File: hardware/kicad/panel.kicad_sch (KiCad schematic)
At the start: 1 part

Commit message: Schematic: panel sheet with 48 lamps
6x 74HC595 (U14-U19) sinking 48 lamps (D7-D54) from VLED through 2k2 x4
arrays (RN1-RN12); chain via QH' local labels; OE_N pull-up. Lamp order
matches firmware/src/panel.h. Custom 595 symbol puts ~SRCLR on top so it
ties to +3V3 without crossings. check.py no longer has pending nets.

Co-Authored-By: Claude Opus 5.5 <noreply@anthropic.com>
Claude-Session: https://claude.ai/code/session_01YRUiF8Vp4242sya9Xyg3TV
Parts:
- added C41, C42, C43, C44, C45, C46: 100nF/16V/10%, Capacitor_SMD:C_0603_1608Metric, symbol Device:C
- added D10, D11, D12, D13, D14, D15, D16, D17, D18, D19, D20, D21, D22, D23, D24, D25, D26, D27, D28, D29, D30, D43, D7, D8, D9: AMBER(0603), LED_SMD:LED_0603_1608Metric, symbol Device:LED
- added D31, D32, D41, D42, D44, D51, D53: YELLOW(0603), LED_SMD:LED_0603_1608Metric, symbol Device:LED
- added D33, D40, D45, D48, D49: GREEN(0603), LED_SMD:LED_0603_1608Metric, symbol Device:LED
- added D34, D35, D36, D37, D38, D39, D46, D47, D50, D52, D54: RED(0603), LED_SMD:LED_0603_1608Metric, symbol Device:LED
- added RN1, RN10, RN11, RN12, RN2, RN3, RN4, RN5, RN6, RN7, RN8, RN9: 2k2x4/5%(CAY16), Resistor_SMD:R_Array_Convex_4x0603, symbol Device:R_Pack04
- added U14, U15, U16, U17, U18, U19: 74HC595PW(TSSOP16), Package_SO:TSSOP-16_4.4x5mm_P0.65mm, symbol coaxolotl:74HC595
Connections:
- net +3V3: now also C41.1, C42.1, C43.1, C44.1, C45.1, C46.1, U14.10 (~{SRCLR}), U14.16 (VCC), U15.10 (~{SRCLR}), U15.16 (VCC), U16.10 (~{SRCLR}), U16.16 (VCC), U17.10 (~{SRCLR}), U17.16 (VCC), U18.10 (~{SRCLR}), U18.16 (VCC), U19.10 (~{SRCLR}), U19.16 (VCC)
- net LED_OE_N: now also U14.13 (~{OE}), U15.13 (~{OE}), U16.13 (~{OE}), U17.13 (~{OE}), U18.13 (~{OE}), U19.13 (~{OE})
- net LED_RCK: now also U14.12 (RCLK), U15.12 (RCLK), U16.12 (RCLK), U17.12 (RCLK), U18.12 (RCLK), U19.12 (RCLK)
- net LED_SCK: now also U14.11 (SRCLK), U15.11 (SRCLK), U16.11 (SRCLK), U17.11 (SRCLK), U18.11 (SRCLK), U19.11 (SRCLK)
- net LED_SER: now also U14.14 (SER)
- new net: D19.1 (K), RN4.8 (R1.2)
- new net: D22.1 (K), RN4.5 (R4.2)
- new net: D18.1 (K), RN3.5 (R4.2)
- new net: D24.1 (K), RN5.7 (R2.2)
- new net: D10.1 (K), RN1.5 (R4.2)
- new net: RN12.1 (R1.1), U19.4 (QE)
- new net: RN12.2 (R2.1), U19.5 (QF)
- new net: RN12.3 (R3.1), U19.6 (QG)
- new net: RN12.4 (R4.1), U19.7 (QH)
- new net: D54.1 (K), RN12.5 (R4.2)
- new net: D53.1 (K), RN12.6 (R3.2)
- new net: D52.1 (K), RN12.7 (R2.2)
- new net: D51.1 (K), RN12.8 (R1.2)
- new net: D39.1 (K), RN9.8 (R1.2)
- new net: D21.1 (K), RN4.6 (R3.2)
- new net: D46.1 (K), RN10.5 (R4.2)
- new net: RN10.1 (R1.1), U18.4 (QE)
- new net: RN10.2 (R2.1), U18.5 (QF)
- new net: RN10.3 (R3.1), U18.6 (QG)
- new net: RN10.4 (R4.1), U18.7 (QH)
- new net: D45.1 (K), RN10.6 (R3.2)
- new net: D44.1 (K), RN10.7 (R2.2)
- new net: D43.1 (K), RN10.8 (R1.2)
- new net: D16.1 (K), RN3.7 (R2.2)
- new net: D9.1 (K), RN1.6 (R3.2)
- new net: D42.1 (K), RN9.5 (R4.2)
- new net: D33.1 (K), RN7.6 (R3.2)
- new net: D32.1 (K), RN7.7 (R2.2)
- new net: RN9.1 (R1.1), U18.15 (QA)
- new net: RN9.2 (R2.1), U18.1 (QB)
- new net: RN9.3 (R3.1), U18.2 (QC)
- new net: RN9.4 (R4.1), U18.3 (QD)
- new net: D41.1 (K), RN9.6 (R3.2)
- new net: D40.1 (K), RN9.7 (R2.2)
- new net: D28.1 (K), RN6.7 (R2.2)
- new net: RN7.1 (R1.1), U17.15 (QA)
- new net: RN7.2 (R2.1), U17.1 (QB)
- new net: RN7.3 (R3.1), U17.2 (QC)
- new net: RN7.4 (R4.1), U17.3 (QD)
- new net: D34.1 (K), RN7.5 (R4.2)
- new net: D31.1 (K), RN7.8 (R1.2)
- new net: RN4.1 (R1.1), U15.4 (QE)
- new net: RN4.2 (R2.1), U15.5 (QF)
- new net: RN4.3 (R3.1), U15.6 (QG)
- new net: RN4.4 (R4.1), U15.7 (QH)
- new net: D20.1 (K), RN4.7 (R2.2)
- new net: RN11.1 (R1.1), U19.15 (QA)
- new net: RN11.2 (R2.1), U19.1 (QB)
- new net: RN11.3 (R3.1), U19.2 (QC)
- new net: RN11.4 (R4.1), U19.3 (QD)
- new net: D50.1 (K), RN11.5 (R4.2)
- new net: D49.1 (K), RN11.6 (R3.2)
- new net: D48.1 (K), RN11.7 (R2.2)
- new net: D47.1 (K), RN11.8 (R1.2)
- new net: RN1.2 (R2.1), U14.1 (QB)
- new net: RN1.1 (R1.1), U14.15 (QA)
- new net: RN1.3 (R3.1), U14.2 (QC)
- new net: RN1.4 (R4.1), U14.3 (QD)
- new net: RN2.1 (R1.1), U14.4 (QE)
- new net: RN2.2 (R2.1), U14.5 (QF)
- new net: RN2.3 (R3.1), U14.6 (QG)
- new net: RN2.4 (R4.1), U14.7 (QH)
- new net: RN8.1 (R1.1), U17.4 (QE)
- new net: RN8.2 (R2.1), U17.5 (QF)
- new net: RN8.3 (R3.1), U17.6 (QG)
- new net: RN8.4 (R4.1), U17.7 (QH)
- new net: D14.1 (K), RN2.5 (R4.2)
- new net: RN3.1 (R1.1), U15.15 (QA)
- new net: RN3.2 (R2.1), U15.1 (QB)
- new net: RN3.3 (R3.1), U15.2 (QC)
- new net: RN3.4 (R4.1), U15.3 (QD)
- new net: D17.1 (K), RN3.6 (R3.2)
- new net: D15.1 (K), RN3.8 (R1.2)
- new net: D29.1 (K), RN6.6 (R3.2)
- new net: D36.1 (K), RN8.7 (R2.2)
- new net: D8.1 (K), RN1.7 (R2.2)
- new net: D26.1 (K), RN5.5 (R4.2)
- new net: D38.1 (K), RN8.5 (R4.2)
- new net: D37.1 (K), RN8.6 (R3.2)
- new net: D35.1 (K), RN8.8 (R1.2)
- new net: D7.1 (K), RN1.8 (R1.2)
- new net: D27.1 (K), RN6.8 (R1.2)
- new net: D25.1 (K), RN5.6 (R3.2)
- new net: RN5.2 (R2.1), U16.1 (QB)
- new net: RN5.1 (R1.1), U16.15 (QA)
- new net: RN5.3 (R3.1), U16.2 (QC)
- new net: RN5.4 (R4.1), U16.3 (QD)
- new net: RN6.1 (R1.1), U16.4 (QE)
- new net: RN6.2 (R2.1), U16.5 (QF)
- new net: RN6.3 (R3.1), U16.6 (QG)
- new net: RN6.4 (R4.1), U16.7 (QH)
- new net: D13.1 (K), RN2.6 (R3.2)
- new net: D12.1 (K), RN2.7 (R2.2)
- new net: D11.1 (K), RN2.8 (R1.2)
- new net: D23.1 (K), RN5.8 (R1.2)
- new net: D30.1 (K), RN6.5 (R4.2)
- new net GND: C41.2, C42.2, C43.2, C44.2, C45.2, C46.2, U14.8 (GND), U15.8 (GND), U16.8 (GND), U17.8 (GND), U18.8 (GND), U19.8 (GND)
- new net LED_CH1: U14.9 (QH'), U15.14 (SER)
- new net LED_CH2: U15.9 (QH'), U16.14 (SER)
- new net LED_CH3: U16.9 (QH'), U17.14 (SER)
- new net LED_CH4: U17.9 (QH'), U18.14 (SER)
- new net LED_CH5: U18.9 (QH'), U19.14 (SER)
- new net VLED: D10.2 (A), D11.2 (A), D12.2 (A), D13.2 (A), D14.2 (A), D15.2 (A), D16.2 (A), D17.2 (A), D18.2 (A), D19.2 (A), D20.2 (A), D21.2 (A), D22.2 (A), D23.2 (A), D24.2 (A), D25.2 (A), D26.2 (A), D27.2 (A), D28.2 (A), D29.2 (A), D30.2 (A), D31.2 (A), D32.2 (A), D33.2 (A), D34.2 (A), D35.2 (A), D36.2 (A), D37.2 (A), D38.2 (A), D39.2 (A), D40.2 (A), D41.2 (A), D42.2 (A), D43.2 (A), D44.2 (A), D45.2 (A), D46.2 (A), D47.2 (A), D48.2 (A), D49.2 (A), D50.2 (A), D51.2 (A), D52.2 (A), D53.2 (A), D54.2 (A), D7.2 (A), D8.2 (A), D9.2 (A)
- no-connect marks 0 -> 1
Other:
- note added: "0 F0 THRU"
- note added: "1 F1 LF"
- note added: "10 FR2 SYNC"
- note added: "11 FR3 B2"
- note added: "12 FR4 B1"
- note added: "13 FR5 B0"
- note added: "14 FR6 LNA"
- note added: "15 FR7 QUIET"
- note added: "16 FR8 CLR"
- note added: "17 FR9 CHK"
- note added: "18 FR10 CHK"
- note added: "19 FR11 CHK"
- note added: "2 F2 160/80"
- note added: "20 FR12 CHK"
- note added: "21 FR13 CHK"
- note added: "22 FR14 CHK"
- note added: "23 RX"
- note added: "24 0"
- note added: "25 1"
- note added: "26 OK"
- note added: "27 ERR"
- note added: "28 SYNC"
- note added: "29 CHK"
- note added: "3 F3 60-30"
- note added: "30 GAP"
- note added: "31 RUNT"
- note added: "32 TMO"
- note added: "33 LNA"
- note added: "34 BYP"
- note added: "35 AUTO"
- note added: "36 FMN"
- note added: "37 I-LO"
- note added: "38 I-OK"
- note added: "39 I-HI"
- note added: "4 F4 20-10"
- note added: "40 TRIP"
- note added: "41 RUN"
- note added: "42 HOLD"
- note added: "43 LOW"
- note added: "44 QUIET"
- note added: "45 DROP"
- note added: "46 GLT"
- note added: "47 RST"
- note added: "5 F5 6/4m"
- note added: "6 F6 2m/AIR"
- note added: "7 F7 70/23cm"
- note added: "8 FR0 SYNC"
- note added: "9 FR1 SYNC"
- note added: "BANK (lamps 0-7)"
- note added: "DECODE (lamps 24-31)"
- note added: "DECODE + RF (lamps 32-39)"
- note added: "FRAME (lamps 8-15)"
- note added: "FRAME + RX (lamps 16-23)"
- note added: "Lamp n: register n/8 (U14 = first after the MCU), output Q(n%8) - firmware/src/panel.h."
- note added: "Lamp test lights all 48 (48 mA) with the LNA still off. Outside it, at most 23 lamps."
- note added: "OE_N pull-up"
- note added: "Q low = lamp on (sink). 1 mA per lamp: (VLED - 2 V - 0.1 V) / 2k2. Use 2 V LEDs only."
- note added: "RF + SYSTEM (lamps 40-47)"
- note removed: "Lamp chain inputs"
- note removed: "NEXT REVIEW: 6x 74HC595 (sinking), 48 lamps on VLED, 2.2k arrays."

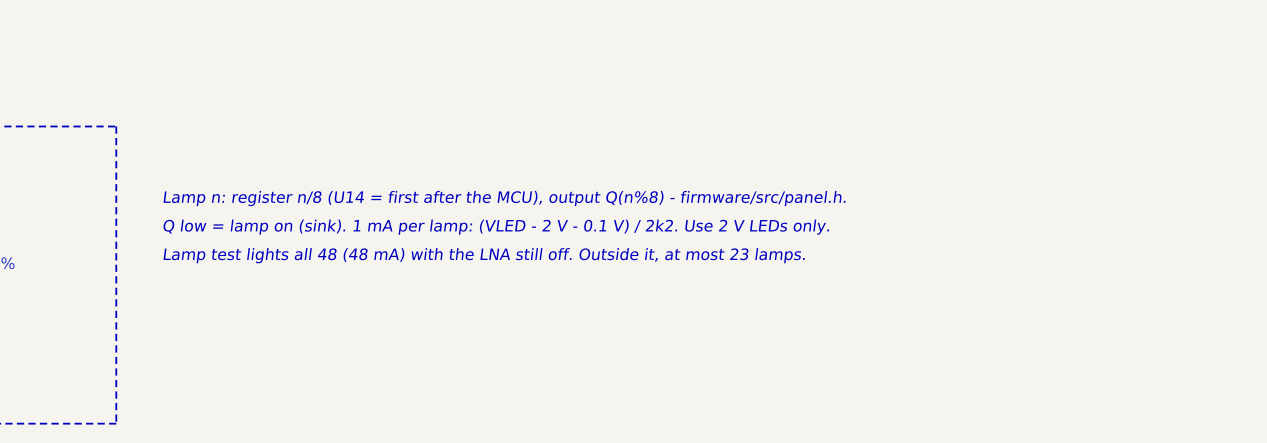
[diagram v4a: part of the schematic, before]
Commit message: Panel modes: full / bands / off via a config frame
- New config frame: sync 0 1 0, payload PM1 PM0 + 4 reserved bits, same
  inverse check. The decoder tells it from the state frame (1 0 1) with
  the same 1.5x ratio test; old hosts keep working.
- full = all 48 lamps, bands = F0..F7 only, off = all dark (OE_N high),
  PWR lamp stays. Outside full nothing blinks, so the MCU sleeps more.
- The mode is logged in flash (page 0x3C00, one byte per change) and
  restored at power-up; the lamp test follows it. Code limit 0x3C00.
- Host: `coaxolotl.py panel full|bands|off` and ConfigFrame.
- 29 new firmware checks (179 total), host end-to-end tests.

Co-Authored-By: Claude Opus 5.5 <noreply@anthropic.com>
Claude-Session: https://claude.ai/code/session_01YRUiF8Vp4242sya9Xyg3TV
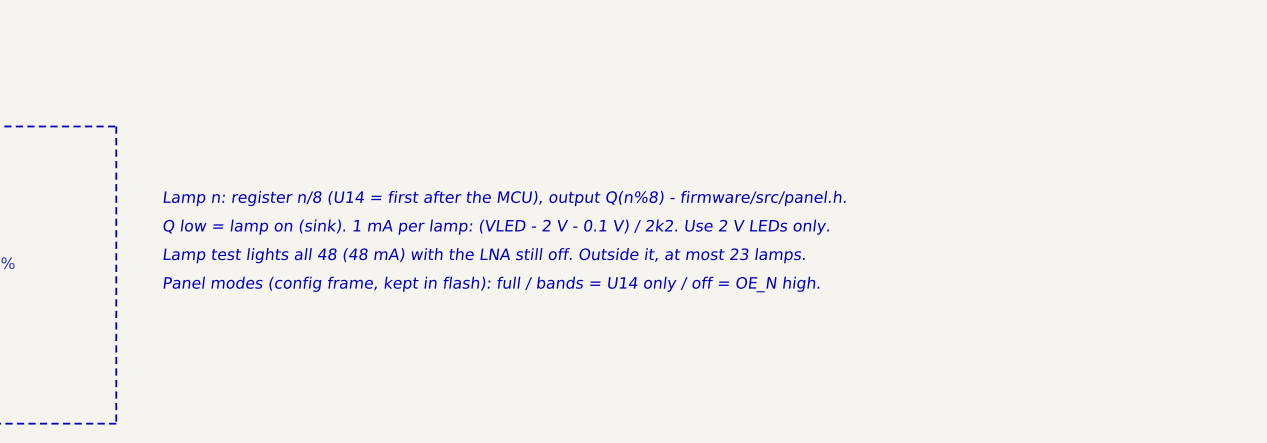
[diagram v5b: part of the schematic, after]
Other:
- note added: "Panel modes (config frame, kept in flash): full / bands = U14 only / off = OE_N high."

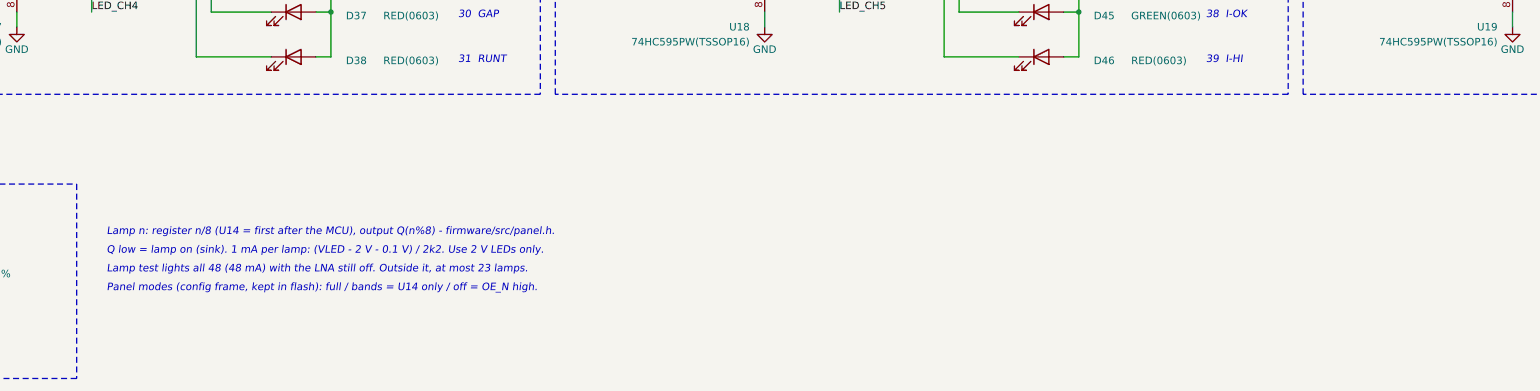
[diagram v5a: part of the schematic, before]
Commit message: Schematic: real F1-F7 LC filters, snap-off lamp strip link
- tools/filters.py: 5th-order Chebyshev 0.1 dB ladders, 50 ohm, E12;
  BPF = HPF + LPF; prints the rounded-value response. F5 is now 30-80 MHz
  (12 dB at 98 MHz instead of 1 dB), bandplan.json updated.
- Filter bank sheet redrawn around the ladders (C1xx..C7xx, L1xx..L7xx).
- Panel sheet: J4/J5 unpopulated 1x7 rows at the right end of the break
  line, so a snapped-off lamp strip can be re-linked with a cable.
- BOM regenerated (224 parts).

Co-Authored-By: Claude Opus 5.5 <noreply@anthropic.com>
Claude-Session: https://claude.ai/code/session_01YRUiF8Vp4242sya9Xyg3TV
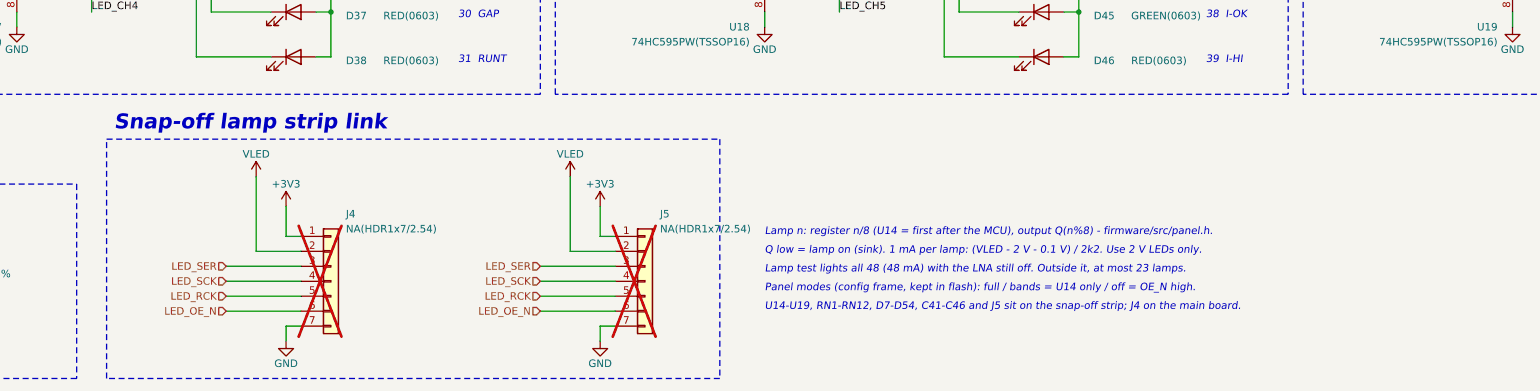
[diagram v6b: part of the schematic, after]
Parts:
- added J4, J5: NA(HDR1x7/2.54), Connector_PinHeader_2.54mm:PinHeader_1x07_P2.54mm_Vertical, symbol Connector_Generic:Conn_01x07
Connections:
- net +3V3: now also J4.1 (Pin_1), J5.1 (Pin_1)
- net GND: now also J4.7 (Pin_7), J5.7 (Pin_7)
- net LED_OE_N: now also J4.6 (Pin_6), J5.6 (Pin_6)
- net LED_RCK: now also J4.5 (Pin_5), J5.5 (Pin_5)
- net LED_SCK: now also J4.4 (Pin_4), J5.4 (Pin_4)
- net LED_SER: now also J4.3 (Pin_3), J5.3 (Pin_3)
- net VLED: now also J4.2 (Pin_2), J5.2 (Pin_2)
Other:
- note added: "Snap-off lamp strip link"
- note added: "U14-U19, RN1-RN12, D7-D54, C41-C46 and J5 sit on the snap-off strip; J4 on the main board."
